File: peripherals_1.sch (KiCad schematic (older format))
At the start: 24 parts, among them J4 JTAG, J5 Molex_0936263508, J6 USB_A, J98 Conn_02x06_Top_Bottom, U6 PCA9546AD, U8 74AC125, U9 TPS2051B

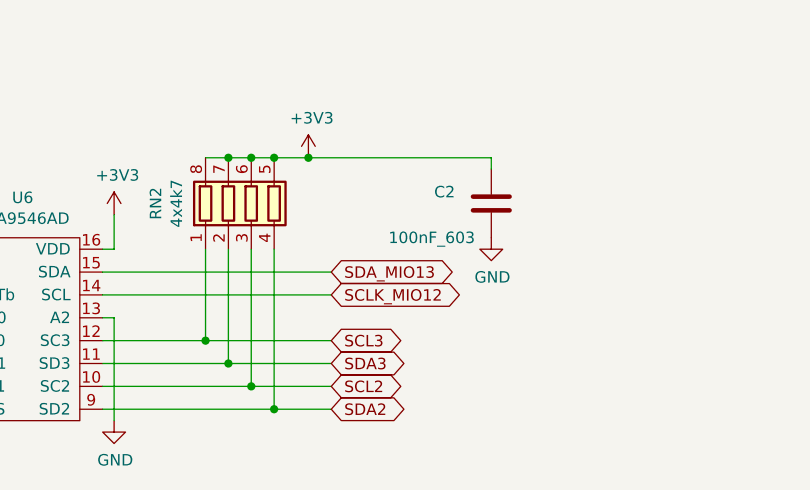
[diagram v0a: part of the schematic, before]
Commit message: re-routed i2c from mio12/13 -> mio10/11
Fixed bug; mio12/13 is used internally on the SOM.
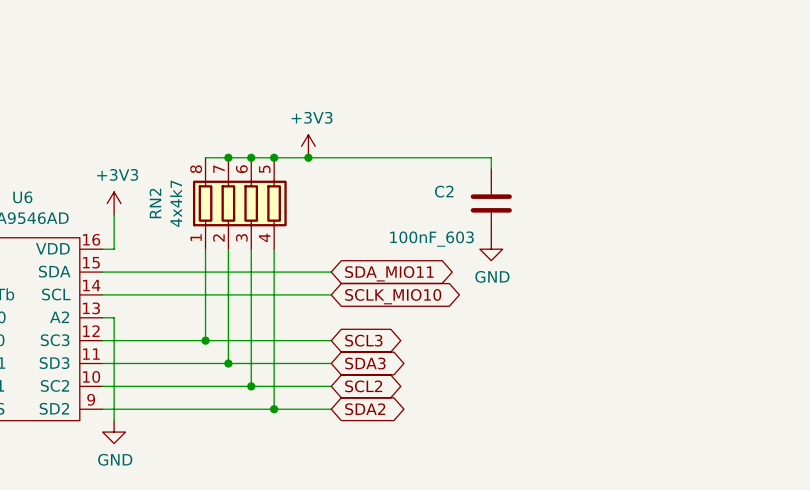
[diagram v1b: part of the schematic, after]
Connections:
- net SCLK_MIO12 renamed SCLK_MIO10
- net SDA_MIO13 renamed SDA_MIO11
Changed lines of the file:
@@
 NoConn ~ 7450 4600
 Text GLabel 4500 6950 2    50   BiDi ~ 0
-SDA_MIO13
+SDA_MIO11
 Text GLabel 4500 7050 2    50   BiDi ~ 0
-SCLK_MIO12
+SCLK_MIO10
 $Comp
 L power:+3V3 #PWR?

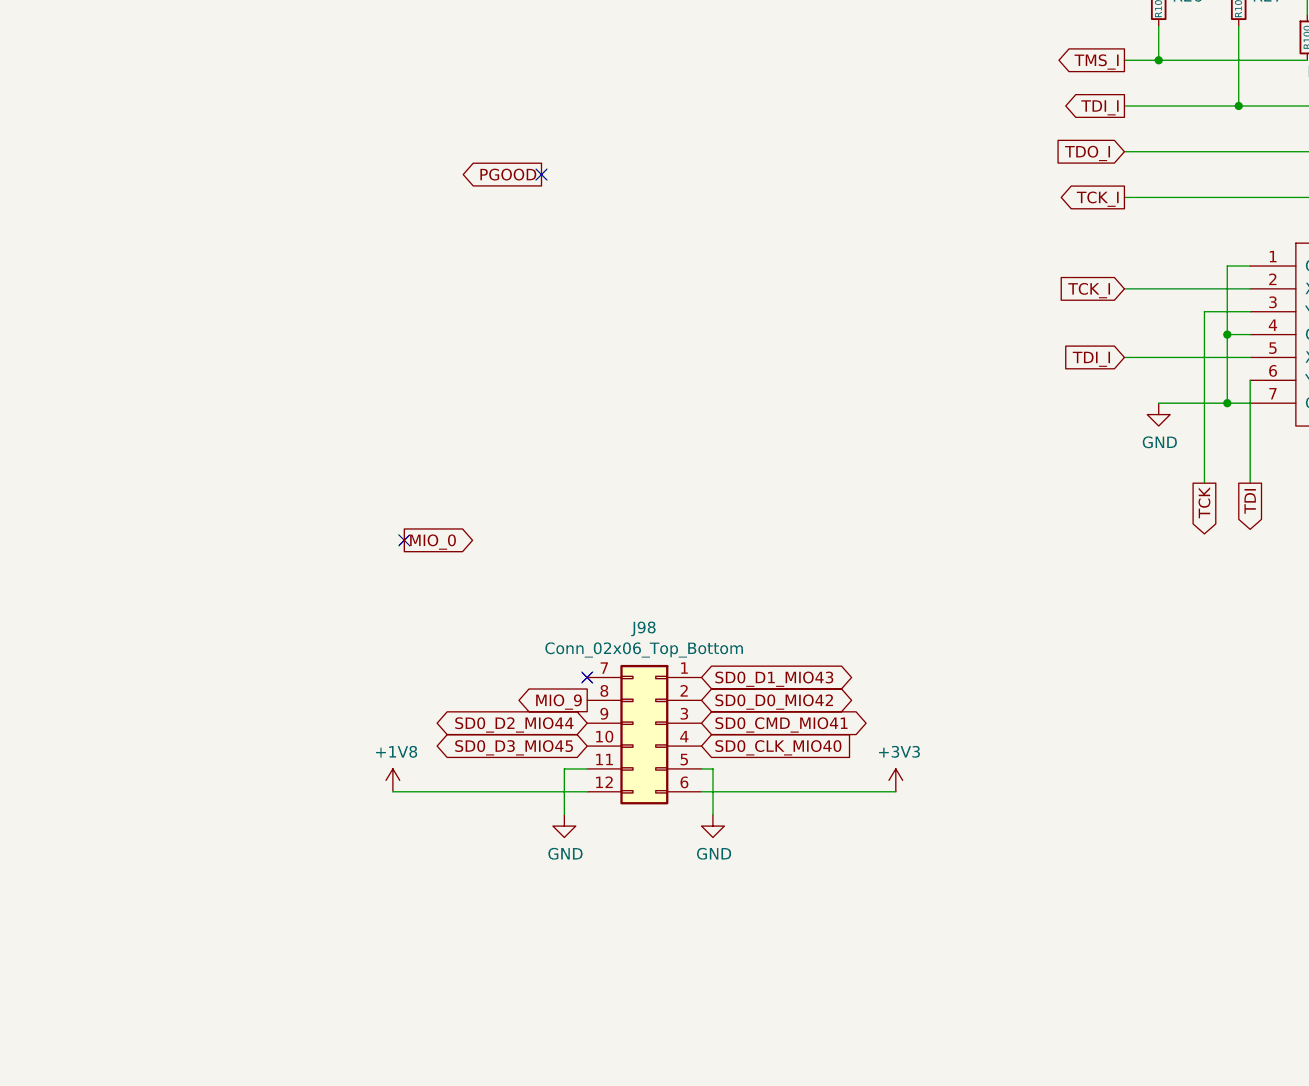
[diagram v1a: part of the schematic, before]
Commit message: hooked up SD-card; use smaller reset button
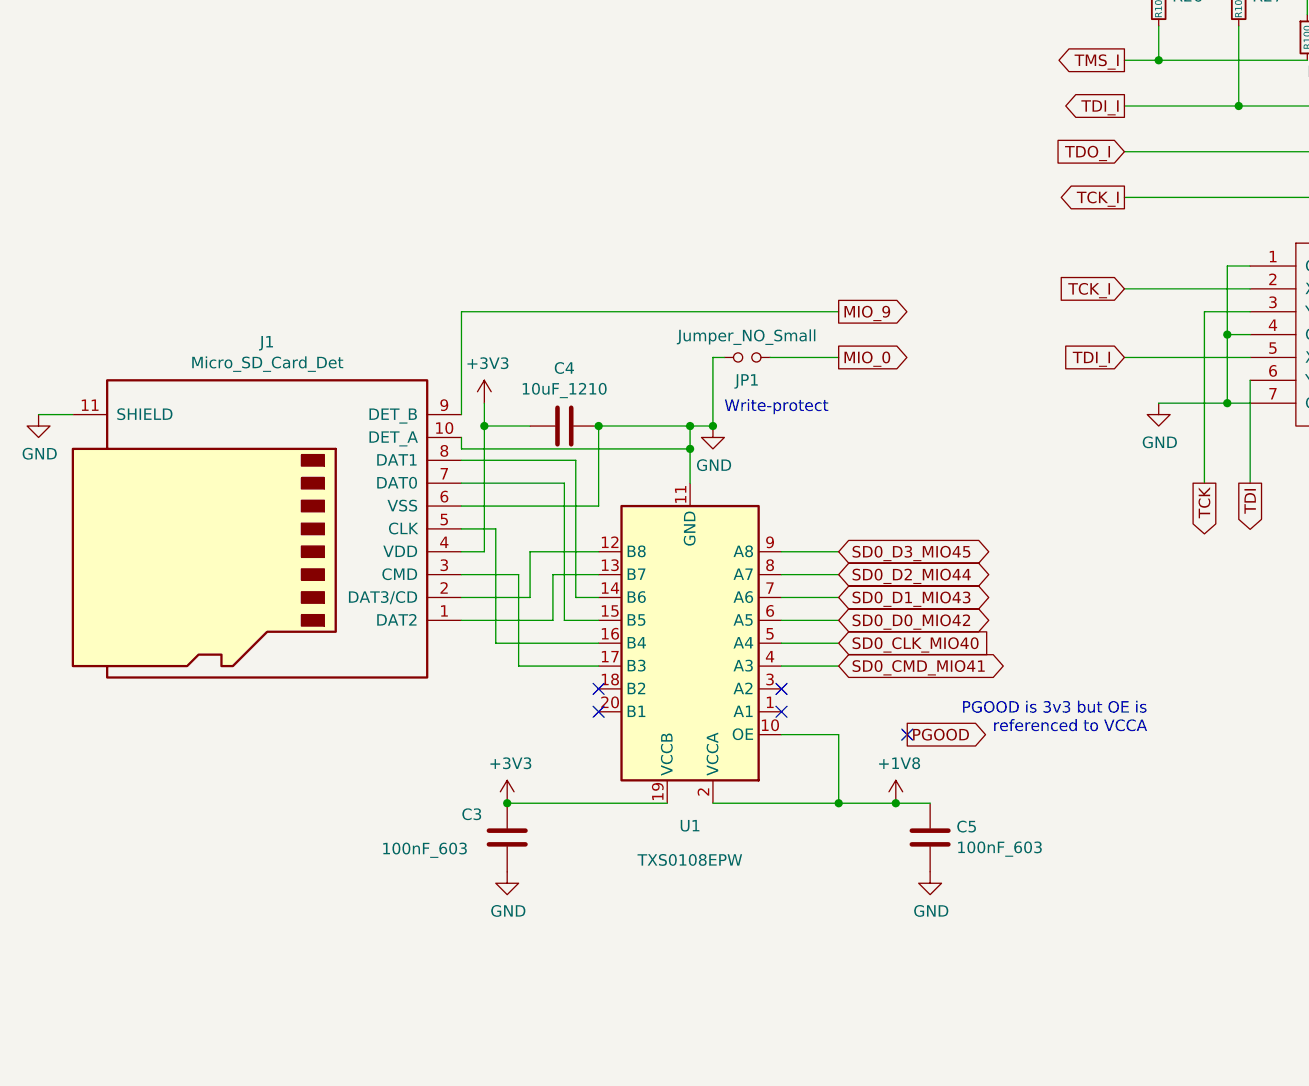
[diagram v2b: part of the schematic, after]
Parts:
- removed J98: Conn_02x06_Top_Bottom, pmod:PinSocket_2x06_P2.54mm_Horizontal, symbol Connector_Generic:Conn_02x06_Top_Bottom
- added C3, C5: 100nF_603, Capacitor_SMD:C_0603_1608Metric, symbol fmc:100nF_603
- added C4: 10uF_1210, Capacitor_SMD:C_1210_3225Metric, symbol fmc:10uF_1210
- added J1: Micro_SD_Card_Det, Connector_Card:microSD_HC_Hirose_DM3D-SF, symbol Connector:Micro_SD_Card_Det
- added JP1: Jumper_NO_Small, Connector_PinHeader_2.54mm:PinHeader_1x02_P2.54mm_Vertical, symbol Device:Jumper_NO_Small
- added U1: TXS0108EPW, Package_SO:TSSOP-20_4.4x6.5mm_P0.65mm, symbol Logic_LevelTranslator:TXS0108EPW
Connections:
- net +1V8: now also C5.1, U1.10 (OE), U1.2 (VCCA)
- net +3V3: now also C3.1, C4.2, J1.4 (VDD), U1.19 (VCCB)
- net GND: now also C3.2, C4.1, C5.2, J1.10 (DET_A), J1.11 (SHIELD), J1.6 (VSS), JP1.1, U1.11 (GND)
- net MIO_0: now also JP1.2
- net MIO_9: now also J1.9 (DET_B)
- net SD0_CLK_MIO40: now also U1.5 (A4)
- net SD0_CMD_MIO41: now also U1.4 (A3)
- net SD0_D0_MIO42: now also U1.6 (A5)
- net SD0_D1_MIO43: now also U1.7 (A6)
- net SD0_D2_MIO44: now also U1.8 (A7)
- net SD0_D3_MIO45: now also U1.9 (A8)
- new net: J1.2 (DAT3/CD), U1.12 (B8)
- new net: J1.1 (DAT2), U1.13 (B7)
- new net: J1.8 (DAT1), U1.14 (B6)
- new net: J1.7 (DAT0), U1.15 (B5)
- new net: J1.5 (CLK), U1.16 (B4)
- new net: J1.3 (CMD), U1.17 (B3)
- no-connect marks 8 -> 10
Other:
- note added: "PGOOD is 3v3 but OE is\nreferenced to VCCA"
- note added: "Write-protect"

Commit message: rotated SDIO to face board front
this allows the power module to be either positioned at its
original location or -- alternatively, next to the SDIO card
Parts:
- J1: footprint Connector_Card:microSD_HC_Hirose_DM3D-SF -> proj_footprints:microSD_HC_Hirose_DM3D-SF_smaller_crtyd
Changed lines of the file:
@@
 F 0 "J1" H 1550 2833 50  0000 C CNN
 F 1 "Micro_SD_Card_Det" H 1550 2924 50  0000 C CNN
-F 2 "Connector_Card:microSD_HC_Hirose_DM3D-SF" H 3650 4350 50  0001 C CNN
+F 2 "proj_footprints:microSD_HC_Hirose_DM3D-SF_smaller_crtyd" H 3650 4350 50  0001 C CNN
 F 3 "https://www.hirose.com/product/en/download_file/key_name/DM3/category/Catalog/doc_file_id/49662/?file_category_id=4&item_id=195&is_series=1" H 1600 3750 50  0001 C CNN
 	1    1600 3650
